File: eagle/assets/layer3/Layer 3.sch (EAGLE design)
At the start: 82 parts, among them Q2 AO3402, X1 SM06B-SRSS-TB, Y1 8MHz

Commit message: Removed Layer 4 and moved all layer 4 to 3
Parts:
- removed 4TH_LAYER: SM04B-SRSS-TB, con-JST SH:SM04B-SRSS-TB
- added COMPASS: BNO055, JH:BNO055
- added R10, R11: 4.7k, SparkFun-Resistors:4.7KOHM-0603-1/10W-1%
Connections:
- removed net RX2_ST3: 4TH_LAYER.1, U$1.10/CS
- removed net RX3_ST2: STM32_IR.PB11/I2C2_SDA/USART3_RX
- removed net TX2_ST3: 4TH_LAYER.2, U$1.9/CS
- removed net TX3_ST2: STM32_IR.PB10/I2C2_SCL/USART3_TX
- new net SCL1: COMPASS.SCL, R11.1, STM32_IR.PB10/I2C2_SCL/USART3_TX
- new net SDA1: COMPASS.SDA, R10.1, STM32_IR.PB11/I2C2_SDA/USART3_RX
- net 3.3V: now also R10.2, R11.2; no longer 4TH_LAYER.4
- net 3V3_SWITCH: now also COMPASS.VCC
- net GND: now also COMPASS.GND; no longer 4TH_LAYER.3
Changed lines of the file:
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@@
 <part name="R8" library="JH" library_urn="urn:adsk.eagle:library:6027132" deviceset="RESISTOR" device="0603" package3d_urn="urn:adsk.eagle:package:15441228/3" value="10k"/>
 <part name="R9" library="JH" library_urn="urn:adsk.eagle:library:6027132" deviceset="RESISTOR" device="0603" package3d_urn="urn:adsk.eagle:package:15441228/3" value="10k"/>
-<part name="GND39" library="SparkFun-PowerSymbols" deviceset="GND" device=""/>
-<part name="SUPPLY1" library="SparkFun-PowerSymbols" deviceset="3.3V" device=""/>
-<part name="4TH_LAYER" library="con-JST SH" library_urn="urn:adsk.eagle:library:16859530" deviceset="SM04B-SRSS" device="-TB" package3d_urn="urn:adsk.eagle:package:16859588/2"/>
 <part name="BLUETOOTH" library="JH" library_urn="urn:adsk.eagle:library:6027132" deviceset="HC-05" device="" package3d_urn="urn:adsk.eagle:package:16970951/2"/>
 <part name="GND40" library="SparkFun-PowerSymbols" deviceset="GND" device=""/>
@@
 <part name="SUPPLY3" library="SparkFun-PowerSymbols" deviceset="5V" device=""/>
 <part name="J1" library="Connectors" library_urn="urn:adsk.eagle:library:19813715" deviceset="CONN_02" device="LOCK" package3d_urn="urn:adsk.eagle:package:19813850/2"/>
+<part name="FRAME7" library="SparkFun-Aesthetics" library_urn="urn:adsk.eagle:library:507" deviceset="FRAME-A4L" device=""/>
+<part name="COMPASS" library="JH" library_urn="urn:adsk.eagle:library:6027132" deviceset="BNO055" device="" package3d_urn="urn:adsk.eagle:package:16833735/3"/>
+<part name="SUPPLY4" library="SparkFun-PowerSymbols" deviceset="3.3V" device=""/>
+<part name="SUPPLY5" library="SparkFun-PowerSymbols" deviceset="3.3V" device=""/>
+<part name="R10" library="SparkFun-Resistors" library_urn="urn:adsk.eagle:library:532" deviceset="4.7KOHM" device="-0603-1/10W-1%" package3d_urn="urn:adsk.eagle:package:39650/1" value="4.7k"/>
+<part name="R11" library="SparkFun-Resistors" library_urn="urn:adsk.eagle:library:532" deviceset="4.7KOHM" device="-0603-1/10W-1%" package3d_urn="urn:adsk.eagle:package:39650/1" value="4.7k"/>
+<part name="GND34" library="SparkFun-PowerSymbols" library_urn="urn:adsk.eagle:library:530" deviceset="GND" device=""/>
 </parts>
 <sheets>
@@
 </segment>
 </net>
-<net name="TX3_ST2" class="0">
+<net name="SCL1" class="0">
 <segment>
 <pinref part="STM32_IR" gate="G$1" pin="PB10/I2C2_SCL/USART3_TX"/>
@@
 </segment>
 </net>
-<net name="RX3_ST2" class="0">
+<net name="SDA1" class="0">
 <segment>
 <pinref part="STM32_IR" gate="G$1" pin="PB11/I2C2_SDA/USART3_RX"/>
@@
 <attribute name="VALUE" x="57.404" y="58.42" size="1.778" layer="96" font="vector" rot="R90" align="top-center"/>
 </instance>
-<instance part="GND39" gate="1" x="66.04" y="78.74" smashed="yes">
-<attribute name="VALUE" x="66.04" y="78.486" size="1.778" layer="96" align="top-center"/>
-</instance>
-<instance part="SUPPLY1" gate="G$1" x="60.96" y="88.9" smashed="yes">
-<attribute name="VALUE" x="60.96" y="91.694" size="1.778" layer="96" align="bottom-center"/>
-</instance>
-<instance part="4TH_LAYER" gate="G$1" x="40.64" y="83.82" smashed="yes">
-<attribute name="VALUE" x="39.37" y="73.66" size="1.778" layer="96"/>
-<attribute name="NAME" x="39.37" y="89.662" size="1.778" layer="95"/>
-</instance>
 <instance part="BLUETOOTH" gate="G$1" x="220.98" y="96.52" smashed="yes">
 <attribute name="NAME" x="213.36" y="104.902" size="1.778" layer="95"/>
@@
 <wire x1="88.9" y1="137.16" x2="88.9" y2="139.7" width="0.1524" layer="91"/>
 <pinref part="SUPPLY25" gate="G$1" pin="3.3V"/>
-</segment>
-<segment>
-<wire x1="48.26" y1="86.36" x2="60.96" y2="86.36" width="0.1524" layer="91"/>
-<wire x1="60.96" y1="86.36" x2="60.96" y2="88.9" width="0.1524" layer="91"/>
-<pinref part="SUPPLY1" gate="G$1" pin="3.3V"/>
-<pinref part="4TH_LAYER" gate="G$1" pin="4"/>
 </segment>
 <segment>
@@
 </segment>
 <segment>
-<wire x1="48.26" y1="83.82" x2="66.04" y2="83.82" width="0.1524" layer="91"/>
-<wire x1="66.04" y1="83.82" x2="66.04" y2="81.28" width="0.1524" layer="91"/>
-<pinref part="GND39" gate="1" pin="GND"/>
-<pinref part="4TH_LAYER" gate="G$1" pin="3"/>
-</segment>
-<segment>
 <pinref part="BLUETOOTH" gate="G$1" pin="GND"/>
 <wire x1="228.6" y1="96.52" x2="248.92" y2="96.52" width="0.1524" layer="91"/>
@@
 </segment>
 </net>
-<net name="RX2_ST3" class="0">
-<segment>
-<pinref part="U$1" gate="G$1" pin="10/CS"/>
-<wire x1="139.7" y1="114.3" x2="139.7" y2="127" width="0.1524" layer="91"/>
-<label x="139.7" y="114.3" size="1.778" layer="95" rot="R90"/>
-</segment>
-<segment>
-<wire x1="48.26" y1="78.74" x2="58.42" y2="78.74" width="0.1524" layer="91"/>
-<label x="48.26" y="78.74" size="1.778" layer="95"/>
-<pinref part="4TH_LAYER" gate="G$1" pin="1"/>
-</segment>
-</net>
-<net name="TX2_ST3" class="0">
-<segment>
-<pinref part="U$1" gate="G$1" pin="9/CS"/>
-<wire x1="142.24" y1="114.3" x2="142.24" y2="127" width="0.1524" layer="91"/>
-<label x="142.24" y="114.3" size="1.778" layer="95" rot="R90"/>
-</segment>
-<segment>
-<wire x1="48.26" y1="81.28" x2="58.42" y2="81.28" width="0.1524" layer="91"/>
-<label x="48.26" y="81.28" size="1.778" layer="95"/>
-<pinref part="4TH_LAYER" gate="G$1" pin="2"/>
-</segment>
-</net>
 <net name="RX_BT" class="0">
 <segment>
@@
 </segment>
 </net>
+</nets>
+</sheet>
+<sheet>
+<description>Compass</description>
+<plain>
+</plain>
+<instances>
+<instance part="FRAME7" gate="G$1" x="5.08" y="5.08" smashed="yes">
+<attribute name="DRAWING_NAME" x="186.69" y="16.51" size="2.54" layer="94" font="vector"/>
+<attribute name="LAST_DATE_TIME" x="186.69" y="11.43" size="2.286" layer="94" font="vector"/>
+<attribute name="SHEET" x="200.66" y="6.35" size="2.54" layer="94" font="vector"/>
+</instance>
+<instance part="COMPASS" gate="G$1" x="106.68" y="106.68" smashed="yes">
+<attribute name="NAME" x="101.6" y="117.348" size="1.27" layer="95"/>
+</instance>
+<instance part="SUPPLY4" gate="G$1" x="175.26" y="109.22" smashed="yes" rot="R270">
+<attribute name="VALUE" x="178.054" y="109.22" size="1.778" layer="96" rot="R270" align="bottom-center"/>
+</instance>
+<instance part="SUPPLY5" gate="G$1" x="175.26" y="96.52" smashed="yes" rot="R270">
+<attribute name="VALUE" x="178.054" y="96.52" size="1.778" layer="96" rot="R270" align="bottom-center"/>
+</instance>
+<instance part="R10" gate="G$1" x="167.64" y="109.22" smashed="yes">
+<attribute name="NAME" x="167.64" y="110.744" size="1.778" layer="95" font="vector" align="bottom-center"/>
+<attribute name="VALUE" x="167.64" y="107.696" size="1.778" layer="96" font="vector" align="top-center"/>
+</instance>
+<instance part="R11" gate="G$1" x="167.64" y="96.52" smashed="yes">
+<attribute name="NAME" x="167.64" y="98.044" size="1.778" layer="95" font="vector" align="bottom-center"/>
+<attribute name="VALUE" x="167.64" y="94.996" size="1.778" layer="96" font="vector" align="top-center"/>
+</instance>
+<instance part="GND34" gate="1" x="138.938" y="111.76" smashed="yes" rot="R90">
+<attribute name="VALUE" x="141.732" y="111.76" size="1.778" layer="96" rot="R270" align="top-center"/>
+</instance>
+</instances>
+<busses>
+</busses>
+<nets>
+<net name="3V3_SWITCH" class="0">
+<segment>
+<pinref part="COMPASS" gate="G$1" pin="VCC"/>
+<wire x1="119.38" y1="114.3" x2="121.92" y2="114.3" width="0.1524" layer="91"/>
+<wire x1="121.92" y1="114.3" x2="121.92" y2="119.38" width="0.1524" layer="91"/>
+<label x="116.84" y="119.38" size="1.778" layer="95"/>
+</segment>
+</net>
+<net name="3.3V" class="0">
+<segment>
+<pinref part="SUPPLY4" gate="G$1" pin="3.3V"/>
+<wire x1="172.72" y1="109.22" x2="175.26" y2="109.22" width="0.1524" layer="91"/>
+<pinref part="R10" gate="G$1" pin="2"/>
+</segment>
+<segment>
+<pinref part="SUPPLY5" gate="G$1" pin="3.3V"/>
+<wire x1="172.72" y1="96.52" x2="175.26" y2="96.52" width="0.1524" layer="91"/>
+<pinref part="R11" gate="G$1" pin="2"/>
+</segment>
+</net>
+<net name="GND" class="0">
+<segment>
+<pinref part="COMPASS" gate="G$1" pin="GND"/>
+<wire x1="119.38" y1="111.76" x2="136.398" y2="111.76" width="0.1524" layer="91"/>
+<pinref part="GND34" gate="1" pin="GND"/>
+</segment>
+</net>
+<net name="SDA1" class="0">
+<segment>
+<pinref part="COMPASS" gate="G$1" pin="SDA"/>
+<wire x1="119.38" y1="109.22" x2="132.08" y2="109.22" width="0.1524" layer="91"/>
+<label x="119.38" y="109.22" size="1.778" layer="95"/>
+</segment>
+<segment>
+<pinref part="R10" gate="G$1" pin="1"/>
+<wire x1="162.56" y1="109.22" x2="162.56" y2="104.14" width="0.1524" layer="91"/>
+<wire x1="162.56" y1="109.22" x2="162.56" y2="114.3" width="0.1524" layer="91"/>
+<junction x="162.56" y="109.22"/>
+<label x="162.56" y="104.14" size="1.778" layer="95" rot="R90"/>
+</segment>
+</net>
+<net name="SCL1" class="0">
+<segment>
+<pinref part="COMPASS" gate="G$1" pin="SCL"/>
+<wire x1="119.38" y1="106.68" x2="132.08" y2="106.68" width="0.1524" layer="91"/>
+<label x="119.38" y="106.68" size="1.778" layer="95"/>
+</segment>
+<segment>
+<pinref part="R11" gate="G$1" pin="1"/>
+<wire x1="162.56" y1="96.52" x2="162.56" y2="101.6" width="0.1524" layer="91"/>
+<wire x1="162.56" y1="96.52" x2="162.56" y2="91.44" width="0.1524" layer="91"/>
+<junction x="162.56" y="96.52"/>
+<label x="162.56" y="93.98" size="1.778" layer="95" rot="R90"/>
+</segment>
+</net>

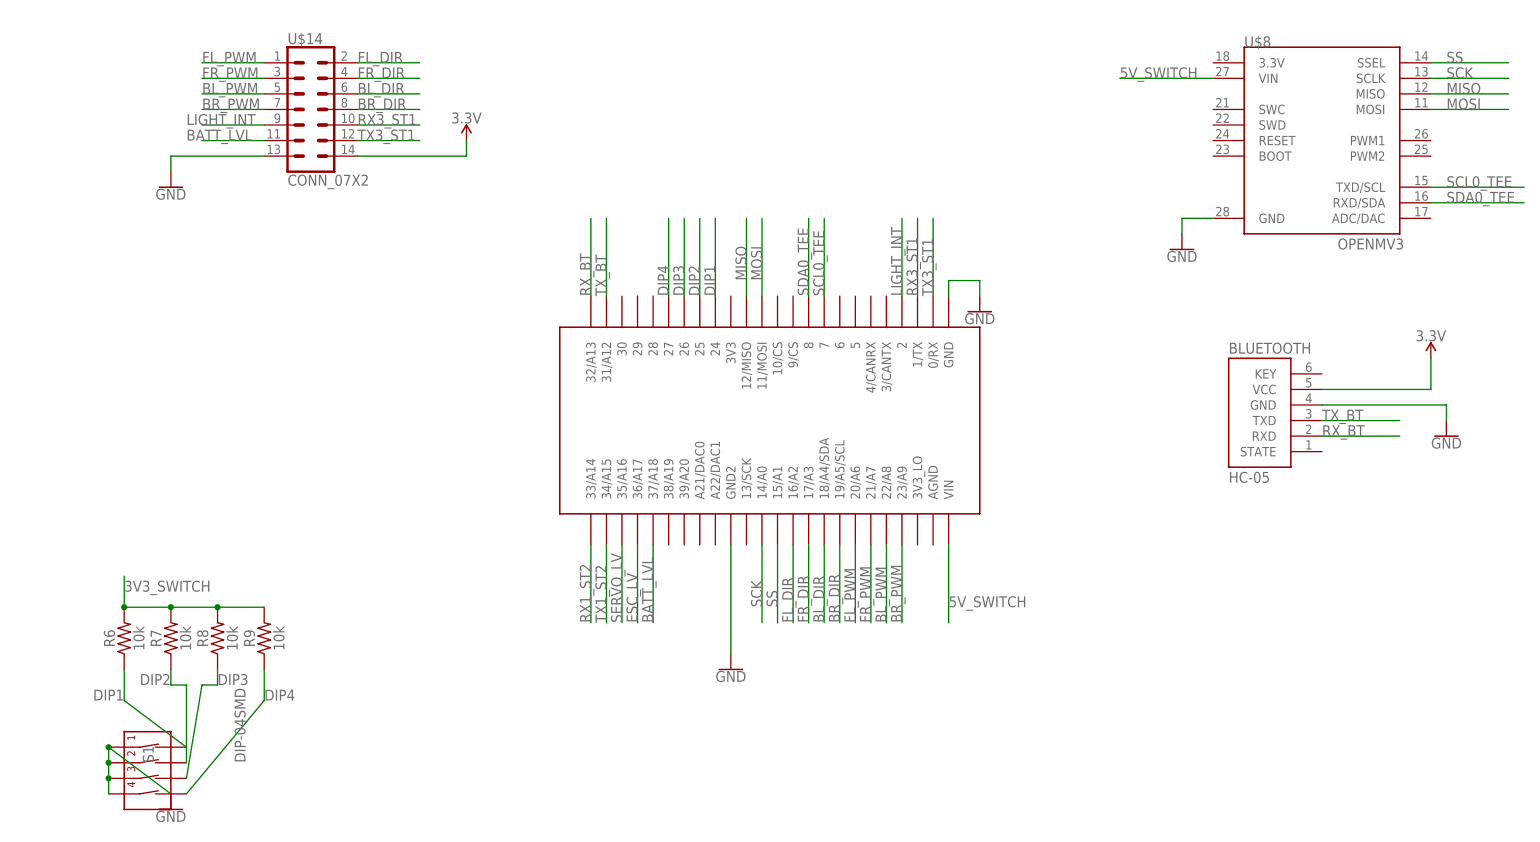
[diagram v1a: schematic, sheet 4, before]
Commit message: Changing 3.6 to 4.0
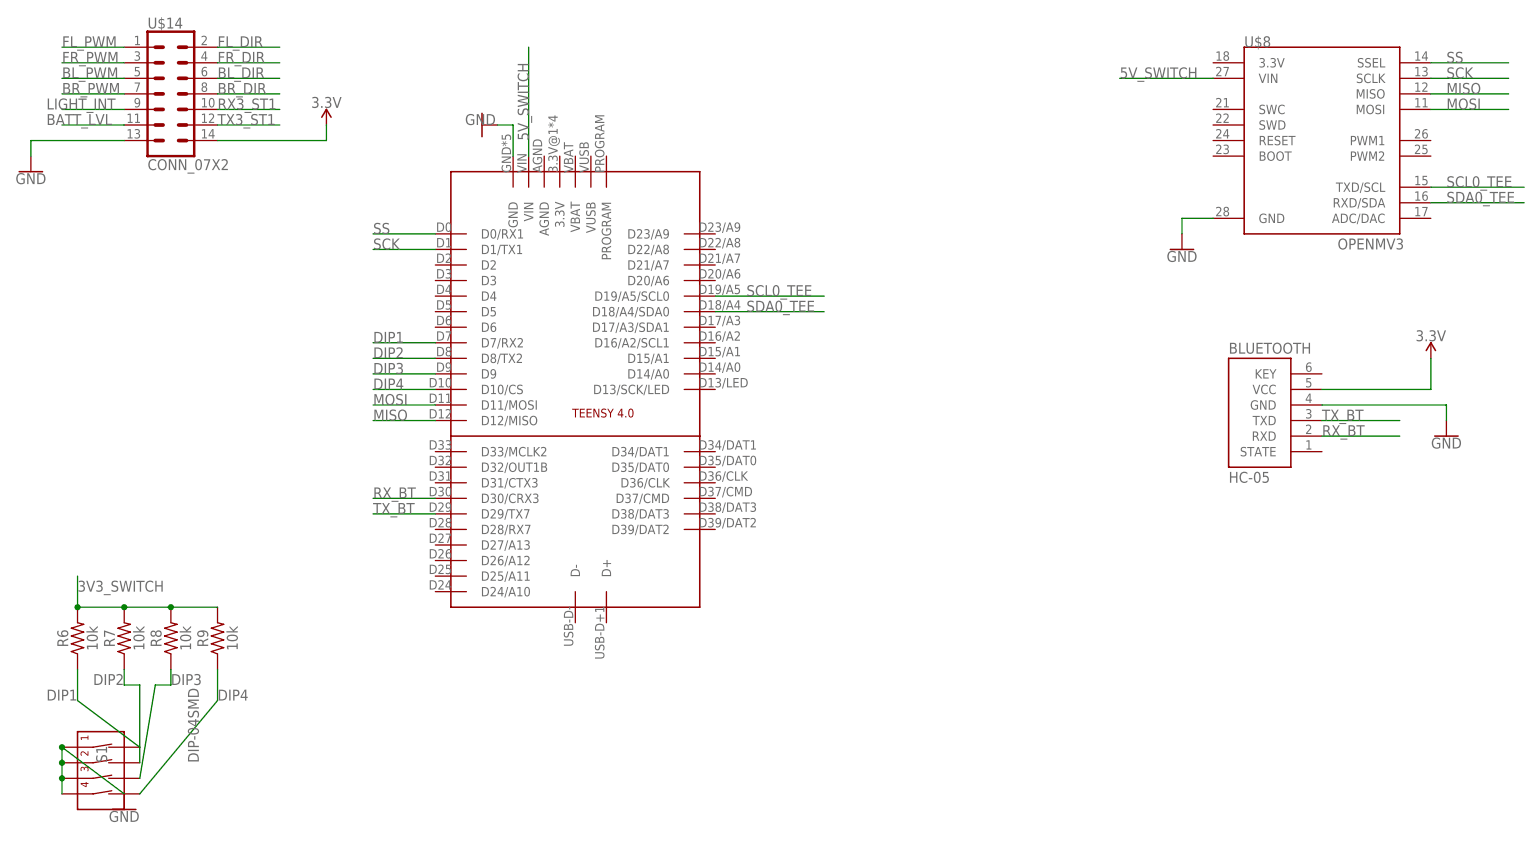
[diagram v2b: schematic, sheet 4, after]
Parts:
- U$1: value TEENSY_3.5/3.6_NO_MIDDLE -> TEENSY-4.0-FULL-BREAKOUT-PINS; device JH:TEENSY_3.5/3.6_NO_MIDDLE -> Teensy-4.0:TEENSY-4.0-FULL-BREAKOUT-PINS
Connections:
- removed net N$1: U$1.GND
- net BATT_LVL: no longer U$1.37/A18
- net BL_DIR: no longer U$1.18/A4/SDA
- net BL_PWM: no longer U$1.22/A8
- net BR_DIR: no longer U$1.19/A5/SCL
- net BR_PWM: no longer U$1.23/A9
- net DIP1: now also U$1.D7/RX2; no longer U$1.24
- net DIP2: now also U$1.D8/TX2; no longer U$1.25
- net DIP3: now also U$1.D9; no longer U$1.26
- net DIP4: now also U$1.D10/CS; no longer U$1.27
- net ESC_LV: no longer U$1.36/A17
- net FL_DIR: no longer U$1.16/A2
- net FL_PWM: no longer U$1.20/A6
- net FR_DIR: no longer U$1.17/A3
- net FR_PWM: no longer U$1.21/A7
- net GND: now also U$1.GND; no longer U$1.GND2
- net LIGHT_INT: no longer U$1.2
- net MISO: now also U$1.D12/MISO; no longer U$1.12/MISO
- net MOSI: now also U$1.D11/MOSI; no longer U$1.11/MOSI
- net RX1_ST2: no longer U$1.33/A14
- net RX3_ST1: no longer U$1.1/TX
- net RX_BT: now also U$1.D30/CRX3; no longer U$1.32/A13
- net SCK: now also U$1.D1/TX1; no longer U$1.14/A0
- net SCL0_TEE: now also U$1.D19/A5/SCL0; no longer U$1.7
- net SDA0_TEE: now also U$1.D18/A4/SDA0; no longer U$1.8
- net SERVO_LV: no longer U$1.35/A16
- net SS: now also U$1.D0/RX1; no longer U$1.15/A1
- net TX1_ST2: no longer U$1.34/A15
- net TX3_ST1: no longer U$1.0/RX
- net TX_BT: now also U$1.D29/TX7; no longer U$1.31/A12
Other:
- moved on the sheet: R6, R7, R8, R9, S1, U$14
